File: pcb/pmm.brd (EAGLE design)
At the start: 30 x 35 mm, 12 parts, among them IC2 REG1117, IC3 STM32F042F4, U2 USBC_16P

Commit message: pcb done
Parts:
- removed JP15, JPAE: (no value), pinhead:1X05
- added C3, C5: 10uF, clock:0805@1
- added C4: 100nF, clock:0805@1
- added LED1, LED2: (no value), adafruit:CHIP-LED0805
- added R3, R5: 10K, joyAnalog:0805
- added R4, R7: 2K, SparkFun-Passives:0805
- added SW3, SW4: 324_SW, 3pos_slide_switch_centered:342_SWICH_FOOT
- added U$3, U$4, U$5, U$6: PINHD5, adafruit_changed:1X05
- C1: value 100nF -> 10uF
- JP1: device pinhead:1X06 -> adafruit:1X06-CLEANBIG
- moved JP1 29.9 mm to (2.16, 11.6), turned to 270 degrees
- moved R2 11.8 mm to (11.4, 25.0), turned to 0 degrees
- moved R1 3.70 mm to (3.43, 25.0), turned to 180 degrees
- moved U2 1.01 mm to (7.49, 31.1)
- moved C2 0.76 mm to (16.0, 28.6)
- moved IC2 0.38 mm to (22.0, 30.1)
- moved C1 0.18 mm to (16.0, 32.8), turned to 90 degrees
- turned IC3 to 180 degrees
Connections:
- removed net DNDNDN: U2.A7, U2.B7
- new net +5V: C1.2, C3.2, C5.2, IC2.3, JP1.5, R3.2, U$1.2, U$1.23, U$2.2, U$2.23, U$5.4, U2.A4B9, U2.B4A9
- new net BUTTON1: IC3.4, SW3.P$2, SW3.P$3
- new net BUTTON2: IC3.1, R5.2, SW4.P$2, SW4.P$3
- new net N$10: IC3.7, JP1.3
- new net N$11: IC3.6, JP1.4
- new net N$12: IC3.2, U$5.2
- new net N$13: IC3.3, U$5.3
- new net N$2: IC3.13, U$1.3
- new net N$29: LED2.C, R7.2
- new net N$3: U$1.22, U$2.3
- new net N$4: IC3.14, R3.1, U$1.24, U$2.24
- new net N$5: LED1.C, R4.2
- new net N$6: IC3.8, U$6.3
- new net N$7: IC3.20, U$6.1
- new net N$8: IC3.19, U$6.2
- new net N$9: IC3.9, JP1.2
- new net USB_DN: IC3.17, U2.A7, U2.B7
- new net USER_LED: IC3.10, R4.1
- net +3V3: now also C4.2, IC3.16, IC3.5, JP1.6, LED1.A, LED2.A, SW4.P$1, SW4.P$4, U$5.5, U$6.4; no longer JP1.4
- net 1: now also U$3.1; no longer JP15.1
- net 2: now also U$3.2; no longer JP15.2
- net 3: now also U$3.3; no longer JP15.3
- net 4: now also U$3.4; no longer JP15.4
- net 5: now also U$3.5; no longer JP15.5
- net A: now also U$4.1; no longer JPAE.1
- net B: now also U$4.2; no longer JPAE.2
- net C: now also U$4.3; no longer JPAE.3
- net E: now also U$4.5; no longer JPAE.5
- net GND: now also C3.1, C4.1, C5.1, IC3.15, JP1.1, R5.1, R7.1, SW3.P$1, SW3.P$4, U$1.21, U$1.4, U$2.21, U$2.4, U$5.1, U$6.5; no longer JP1.5
- net N$1: now also IC3.11, U$1.1, U$2.1; no longer C1.2, IC2.3, U2.A4B9, U2.B4A9
- net USB_DP: now also IC3.18
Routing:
- net +5V: track 0.00 -> 85.0 mm, vias 0 -> 1
- net GND: track 0.00 -> 47.9 mm
- net 3: track 0.00 -> 33.3 mm, vias 0 -> 1
- net 4: track 0.00 -> 30.4 mm, vias 0 -> 2
- net USB_DN: track 0.00 -> 28.8 mm
- net 5: track 0.00 -> 26.0 mm
- net 2: track 0.00 -> 25.6 mm, vias 0 -> 1
- net +3V3: track 0.00 -> 25.5 mm, vias 0 -> 6
- net USB_DP: track 0.00 -> 20.4 mm
- net A: track 0.00 -> 20.2 mm
- net N$13: track 0.00 -> 19.7 mm, vias 0 -> 1
- net E: track 0.00 -> 19.7 mm
- net 1: track 0.00 -> 19.3 mm
- net N$11: track 0.00 -> 18.9 mm, vias 0 -> 1
- net N$4: track 0.00 -> 18.8 mm, vias 0 -> 2
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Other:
- board text added: "1 2 3 4 5"
- board text added: "3"
- board text added: "5"
- board text added: "A B C D E"
- board text added: "A0"
- board text added: "A1"
- board text added: "A4"
- board text added: "C"
- board text added: "D"
- board text added: "F0"
- board text added: "F1"
- board text added: "G"
- board text added: "Pimp-my-microwave dekuNukem JUL2020 PT0"
- board text added: "RX"
- board text added: "T"

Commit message: minor cleanup
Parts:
- renumbered R7 to R6
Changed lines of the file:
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@@
 <setting verticaltext="up"/>
 </settings>
-<grid distance="5" unitdist="mil" unit="mil" style="lines" multiple="1" display="no" altdistance="1" altunitdist="mil" altunit="mil"/>
+<grid distance="5" unitdist="mil" unit="mm" style="lines" multiple="1" display="no" altdistance="1" altunitdist="mil" altunit="mil"/>
 <layers>
 <layer number="1" name="Top" color="4" fill="1" visible="yes" active="yes"/>
@@
 <attribute name="VALUE" x="2.159" y="20.574" size="1.27" layer="27"/>
 </element>
-<element name="R7" library="SparkFun-Passives" package="0805" value="2K" x="8.0518" y="23.495" smashed="yes" rot="R180">
+<element name="R6" library="SparkFun-Passives" package="0805" value="2K" x="8.0518" y="23.495" smashed="yes" rot="R180">
 <attribute name="NAME" x="8.6868" y="25.2095" size="0.8128" layer="25" rot="R180"/>
 </element>
@@
 <contactref element="C2" pad="2"/>
 <polygon width="0.1524" layer="1" isolate="0.254">
-<vertex x="0" y="35.052"/>
+<vertex x="0" y="35"/>
 <vertex x="0" y="0"/>
-<vertex x="29.972" y="0"/>
-<vertex x="29.972" y="35.052"/>
+<vertex x="30" y="0"/>
+<vertex x="30" y="35"/>
 </polygon>
 <contactref element="U$1" pad="4"/>
@@
 <contactref element="SW3" pad="P$1"/>
 <contactref element="SW3" pad="P$4"/>
-<contactref element="R7" pad="1"/>
+<contactref element="R6" pad="1"/>
 <contactref element="R5" pad="1"/>
 <contactref element="U$6" pad="5"/>
@@
 <contactref element="C2" pad="1"/>
 <polygon width="0.1524" layer="16">
-<vertex x="0" y="35.052"/>
-<vertex x="29.972" y="35.052"/>
-<vertex x="29.972" y="0"/>
+<vertex x="0" y="35"/>
+<vertex x="30" y="35"/>
+<vertex x="30" y="0"/>
 <vertex x="0" y="0"/>
 </polygon>
@@
 <signal name="N$29">
 <contactref element="LED2" pad="C"/>
-<contactref element="R7" pad="2"/>
+<contactref element="R6" pad="2"/>
 <wire x1="7.1518" y1="23.495" x2="6.7708" y2="23.114" width="0.1524" layer="1"/>
 <wire x1="6.7708" y1="23.114" x2="4.479" y2="23.114" width="0.1524" layer="1"/>

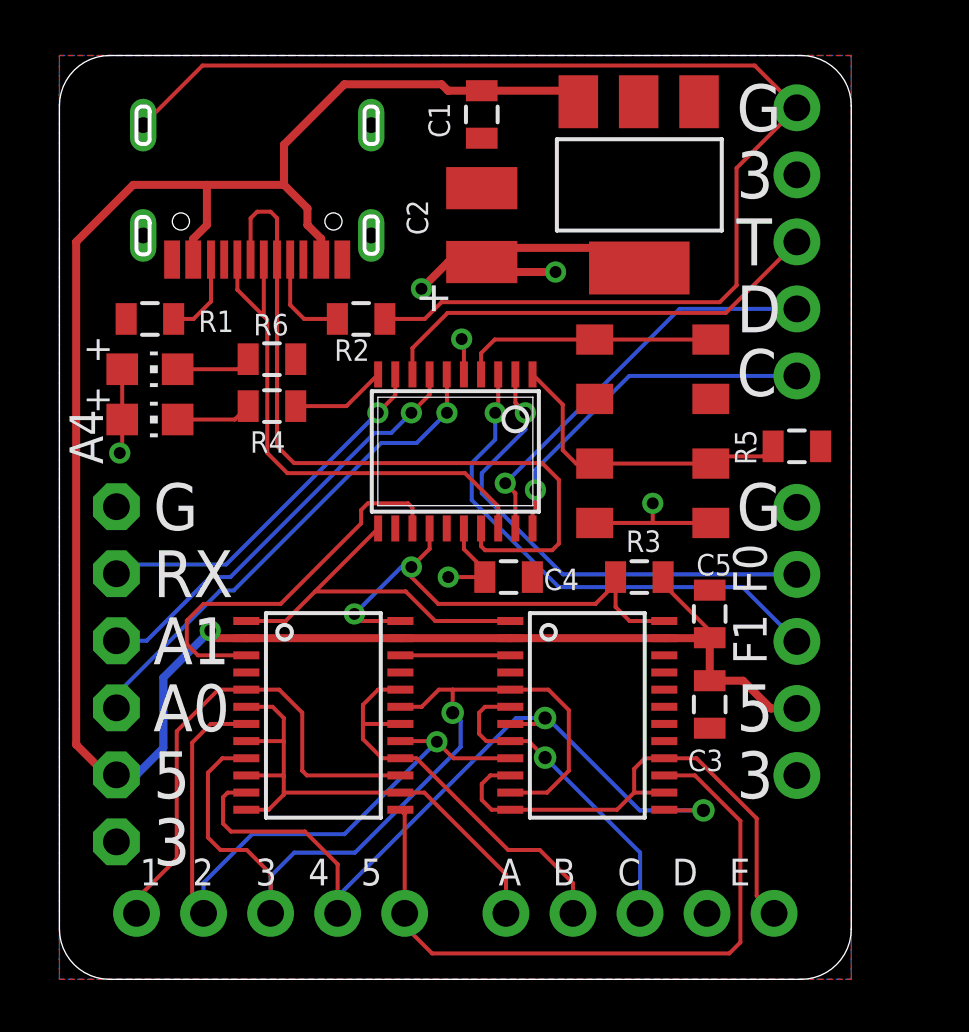
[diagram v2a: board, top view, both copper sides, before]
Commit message: added a required pullup resistor
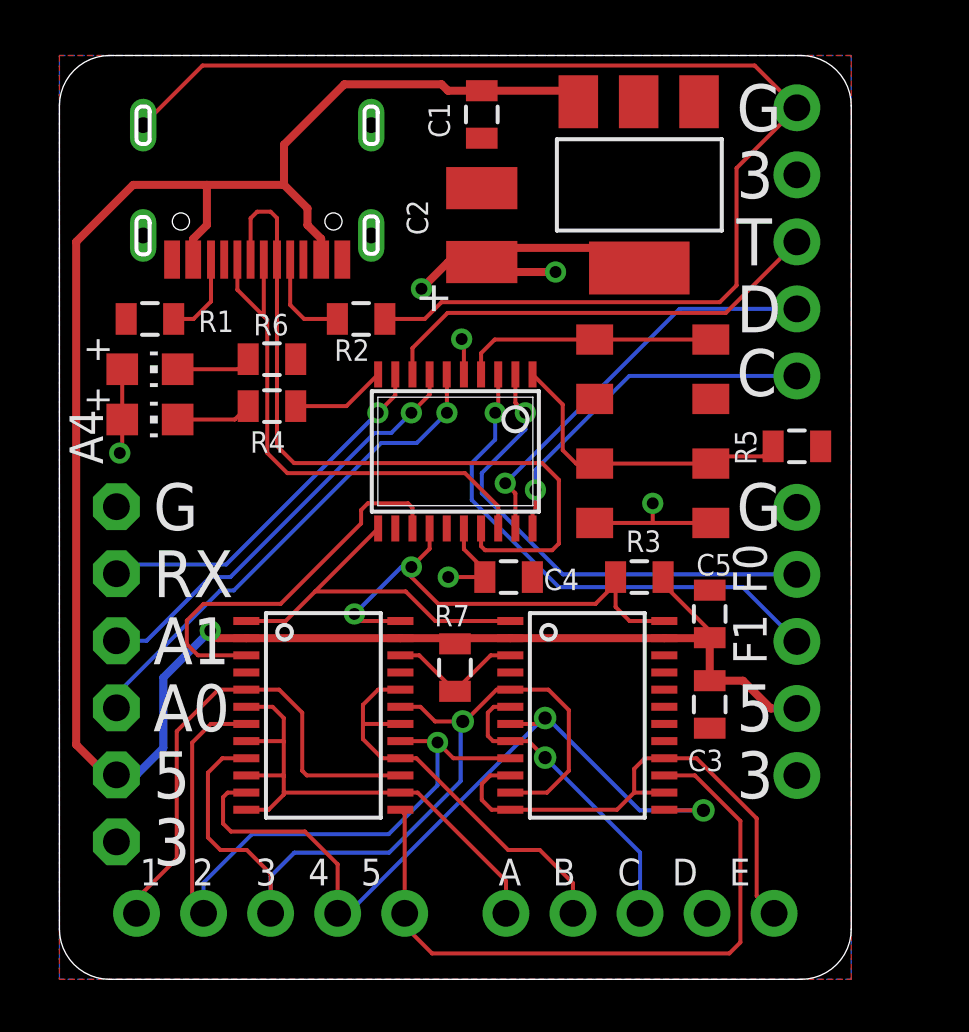
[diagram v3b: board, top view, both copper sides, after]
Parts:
- added R7: 10K, joyAnalog:0805
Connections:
- net +5V: now also R7.2
- net N$3: now also R7.1
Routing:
- net N$3: track 4.16 -> 5.30 mm
- net 2: track 25.6 -> 26.6 mm
- net C: track 12.3 -> 11.7 mm
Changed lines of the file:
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@@
 <setting verticaltext="up"/>
 </settings>
-<grid distance="5" unitdist="mil" unit="mm" style="lines" multiple="1" display="no" altdistance="1" altunitdist="mil" altunit="mil"/>
+<grid distance="1" unitdist="mil" unit="mil" style="lines" multiple="1" display="no" altdistance="1" altunitdist="mil" altunit="mil"/>
 <layers>
 <layer number="1" name="Top" color="4" fill="1" visible="yes" active="yes"/>
@@
 <attribute name="NAME" x="24.13" y="15.3035" size="0.8128" layer="25"/>
 </element>
+<element name="R7" library="joyAnalog" package="0805" value="10K" x="14.986" y="11.811" smashed="yes" rot="R90">
+<attribute name="NAME" x="15.5448" y="14.1859" size="0.8128" layer="25" rot="R180"/>
+</element>
 </elements>
 <signals>
@@
 <wire x1="12.9178" y1="7.075" x2="8.525" y2="7.075" width="0.1524" layer="1"/>
 <wire x1="8.525" y1="7.075" x2="8.5" y2="7.1" width="0.1524" layer="1"/>
-<wire x1="13.825" y1="7.075" x2="12.9178" y2="7.075" width="0.1524" layer="1"/>
-<wire x1="13.825" y1="7.075" x2="16.92" y2="3.98" width="0.1524" layer="1"/>
+<wire x1="13.571" y1="7.075" x2="12.9178" y2="7.075" width="0.1524" layer="1"/>
+<wire x1="13.571" y1="7.075" x2="16.92" y2="3.726" width="0.1524" layer="1"/>
 <contactref element="U$4" pad="1"/>
-<wire x1="16.92" y1="3.98" x2="16.92" y2="2.5036" width="0.1524" layer="1"/>
+<wire x1="16.92" y1="3.726" x2="16.92" y2="2.5036" width="0.1524" layer="1"/>
 <wire x1="16.92" y1="2.5036" x2="16.9164" y2="2.5" width="0.1524" layer="1"/>
 </signal>
@@
 <contactref element="U$2" pad="6"/>
 <contactref element="U$2" pad="8"/>
-<wire x1="17.0822" y1="10.325" x2="16.125" y2="10.325" width="0.1524" layer="1"/>
-<wire x1="16.125" y1="10.325" x2="15.9" y2="10.1" width="0.1524" layer="1"/>
-<wire x1="15.9" y1="10.1" x2="15.9" y2="9.3" width="0.1524" layer="1"/>
-<wire x1="16.175" y1="9.025" x2="17.0822" y2="9.025" width="0.1524" layer="1"/>
-<wire x1="15.9" y1="9.3" x2="16.175" y2="9.025" width="0.1524" layer="1"/>
+<wire x1="17.0822" y1="10.325" x2="16.4552" y2="10.325" width="0.1524" layer="1"/>
+<wire x1="16.4552" y1="10.325" x2="16.2302" y2="10.1" width="0.1524" layer="1"/>
+<wire x1="16.2302" y1="10.1" x2="16.2302" y2="9.2238" width="0.1524" layer="1"/>
+<wire x1="16.429" y1="9.025" x2="17.0822" y2="9.025" width="0.1524" layer="1"/>
+<wire x1="16.2302" y1="9.2238" x2="16.429" y2="9.025" width="0.1524" layer="1"/>
 <wire x1="17.0822" y1="9.025" x2="17.775" y2="9.025" width="0.1524" layer="1"/>
 <wire x1="17.775" y1="9.025" x2="18.4" y2="8.4" width="0.1524" layer="1"/>
@@
 <contactref element="U$1" pad="17"/>
 <contactref element="U$2" pad="9"/>
-<via x="14.3" y="9" extent="1-16" drill="0.45"/>
-<wire x1="14.3" y1="9" x2="10.8" y2="5.5" width="0.1524" layer="16"/>
-<wire x1="10.8" y1="5.5" x2="7.3" y2="5.5" width="0.1524" layer="16"/>
+<via x="14.3254" y="8.9746" extent="1-16" drill="0.45"/>
+<wire x1="14.3254" y1="8.9746" x2="14.3254" y2="7.349" width="0.1524" layer="16"/>
+<wire x1="14.3254" y1="7.349" x2="12.4764" y2="5.5" width="0.1524" layer="16"/>
+<wire x1="12.4764" y1="5.5" x2="7.3" y2="5.5" width="0.1524" layer="16"/>
 <wire x1="7.3" y1="5.5" x2="5.46" y2="3.66" width="0.1524" layer="16"/>
 <wire x1="12.9178" y1="9.025" x2="14.275" y2="9.025" width="0.1524" layer="1"/>
-<wire x1="14.275" y1="9.025" x2="14.3" y2="9" width="0.1524" layer="1"/>
-<wire x1="14.925" y1="8.375" x2="14.3" y2="9" width="0.1524" layer="1"/>
+<wire x1="14.275" y1="9.025" x2="14.3254" y2="8.9746" width="0.1524" layer="1"/>
+<wire x1="14.925" y1="8.375" x2="14.3254" y2="8.9746" width="0.1524" layer="1"/>
 <wire x1="17.0822" y1="8.375" x2="14.925" y2="8.375" width="0.1524" layer="1"/>
 <wire x1="7.0822" y1="9.675" x2="5.738" y2="9.675" width="0.1524" layer="1"/>
@@
 <wire x1="5.627" y1="5.373" x2="6.1" y2="4.9" width="0.1524" layer="1"/>
 <wire x1="6.1" y1="4.9" x2="7.1" y2="4.9" width="0.1524" layer="1"/>
-<wire x1="17.0822" y1="10.975" x2="14.9" y2="10.975" width="0.1524" layer="1"/>
-<wire x1="14.9" y1="10.975" x2="14.375" y2="10.975" width="0.1524" layer="1"/>
-<wire x1="13.725" y1="10.325" x2="12.9178" y2="10.325" width="0.1524" layer="1"/>
-<wire x1="14.375" y1="10.975" x2="13.725" y2="10.325" width="0.1524" layer="1"/>
 <wire x1="17.0822" y1="7.075" x2="18.475" y2="7.075" width="0.1524" layer="1"/>
 <wire x1="18.475" y1="7.075" x2="19.3" y2="7.9" width="0.1524" layer="1"/>
@@
 <wire x1="18.525" y1="10.975" x2="17.0822" y2="10.975" width="0.1524" layer="1"/>
 <wire x1="19.3" y1="10.2" x2="18.525" y2="10.975" width="0.1524" layer="1"/>
-<wire x1="14.9" y1="10.975" x2="14.9" y2="10.1" width="0.1524" layer="1"/>
-<via x="14.9" y="10.1" extent="1-16" drill="0.5"/>
-<wire x1="14.9" y1="10.1" x2="15.2" y2="9.8" width="0.1524" layer="16"/>
-<wire x1="15.2" y1="9.8" x2="15.2" y2="8.8" width="0.1524" layer="16"/>
-<wire x1="15.2" y1="8.8" x2="11.2" y2="4.8" width="0.1524" layer="16"/>
-<wire x1="11.2" y1="4.8" x2="8.9" y2="4.8" width="0.1524" layer="16"/>
+<via x="15.281" y="9.7698" extent="1-16" drill="0.5"/>
+<wire x1="15.281" y1="9.7698" x2="15.2" y2="9.6888" width="0.1524" layer="16"/>
+<wire x1="15.2" y1="9.6888" x2="15.2" y2="7.5046" width="0.1524" layer="16"/>
+<wire x1="15.2" y1="7.5046" x2="12.4954" y2="4.8" width="0.1524" layer="16"/>
+<wire x1="12.4954" y1="4.8" x2="8.9" y2="4.8" width="0.1524" layer="16"/>
 <wire x1="8.9" y1="4.8" x2="8" y2="3.9" width="0.1524" layer="16"/>
 <contactref element="U$3" pad="3"/>
@@
 <wire x1="8" y1="2.501" x2="8.001" y2="2.5" width="0.1524" layer="16"/>
 <wire x1="8.001" y1="3.999" x2="8.001" y2="2.5" width="0.1524" layer="1"/>
+<wire x1="12.9178" y1="10.325" x2="13.678" y2="10.325" width="0.1524" layer="1"/>
+<wire x1="14.2332" y1="9.7698" x2="15.281" y2="9.7698" width="0.1524" layer="1"/>
+<wire x1="13.678" y1="10.325" x2="14.2332" y2="9.7698" width="0.1524" layer="1"/>
+<wire x1="17.0822" y1="10.975" x2="16.563" y2="10.975" width="0.1524" layer="1"/>
+<wire x1="15.3578" y1="9.7698" x2="15.281" y2="9.7698" width="0.1524" layer="1"/>
+<wire x1="16.563" y1="10.975" x2="15.3578" y2="9.7698" width="0.1524" layer="1"/>
 </signal>
 <signal name="4">
@@
 <wire x1="24.4" y1="6.4" x2="22.9428" y2="6.4" width="0.1524" layer="1"/>
 <wire x1="22.9428" y1="6.4" x2="22.9178" y2="6.425" width="0.1524" layer="1"/>
-<wire x1="17.3" y1="9.9" x2="18.4" y2="9.9" width="0.1524" layer="16"/>
-<wire x1="10.54" y1="3.14" x2="17.3" y2="9.9" width="0.1524" layer="16"/>
+<wire x1="18.3414" y1="9.9" x2="18.4" y2="9.9" width="0.1524" layer="16"/>
+<wire x1="18.3414" y1="9.9" x2="10.9414" y2="2.5" width="0.1524" layer="16"/>
+<wire x1="10.541" y1="2.5" x2="10.9414" y2="2.5" width="0.1524" layer="16"/>
 <contactref element="U$3" pad="4"/>
 <wire x1="9.3" y1="5.6" x2="10.541" y2="4.359" width="0.1524" layer="1"/>
 <wire x1="10.541" y1="4.359" x2="10.541" y2="2.5" width="0.1524" layer="1"/>
-<wire x1="10.541" y1="2.5" x2="10.541" y2="3.139" width="0.1524" layer="16"/>
-<wire x1="10.541" y1="3.139" x2="10.54" y2="3.14" width="0.1524" layer="16"/>
 </signal>
 <signal name="5">
@@
 <wire x1="1.778" y1="7.747" x2="2.159" y2="7.747" width="0.3048" layer="1"/>
 <wire x1="22.9178" y1="12.925" x2="17.0822" y2="12.925" width="0.3048" layer="1"/>
-<wire x1="17.0822" y1="12.925" x2="12.9178" y2="12.925" width="0.3048" layer="1"/>
 <wire x1="12.9178" y1="12.925" x2="7.0822" y2="12.925" width="0.3048" layer="1"/>
 <wire x1="7.0822" y1="12.925" x2="5.998" y2="12.925" width="0.3048" layer="1"/>
@@
 <wire x1="24.638" y1="13.208" x2="24.638" y2="12.943" width="0.1524" layer="1"/>
 <wire x1="22.871" y1="14.975" x2="24.638" y2="13.208" width="0.1524" layer="1"/>
+<contactref element="R7" pad="2"/>
+<wire x1="12.9178" y1="12.925" x2="14.772" y2="12.925" width="0.3048" layer="1"/>
+<wire x1="14.772" y1="12.925" x2="14.986" y2="12.711" width="0.3048" layer="1"/>
+<wire x1="17.0822" y1="12.925" x2="15.2" y2="12.925" width="0.3048" layer="1"/>
+<wire x1="15.2" y1="12.925" x2="14.986" y2="12.711" width="0.3048" layer="1"/>
 </signal>
 <signal name="N$1">
@@
 <contactref element="U$1" pad="22"/>
 <contactref element="U$2" pad="3"/>
-<wire x1="12.9178" y1="12.275" x2="17.0822" y2="12.275" width="0.1524" layer="1"/>
+<contactref element="R7" pad="1"/>
+<wire x1="12.9178" y1="12.275" x2="13.633" y2="12.275" width="0.1524" layer="1"/>
+<wire x1="14.986" y1="10.922" x2="14.986" y2="10.911" width="0.1524" layer="1"/>
+<wire x1="13.633" y1="12.275" x2="14.986" y2="10.922" width="0.1524" layer="1"/>
+<wire x1="17.0822" y1="12.275" x2="16.339" y2="12.275" width="0.1524" layer="1"/>
+<wire x1="16.339" y1="12.275" x2="14.986" y2="10.922" width="0.1524" layer="1"/>
 </signal>
 <signal name="N$4">

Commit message: 2nd prototype
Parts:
- moved R7 0.13 mm to (15.0, 11.9)
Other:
- board text added: "Pimp-my-microwave dekuNukem AUG2020 PT1"
- board text removed: "Pimp-my-microwave dekuNukem JUL2020 PT0"
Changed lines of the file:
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@@
 <text x="10.922" y="27.94" size="1.778" layer="22" rot="MR270">Pimp-my-microwave
 dekuNukem
-JUL2020 PT0</text>
+AUG2020 PT1</text>
 </plain>
 <attributes>
@@
 <attribute name="NAME" x="24.13" y="15.3035" size="0.8128" layer="25"/>
 </element>
-<element name="R7" library="joyAnalog" package="0805" value="10K" x="14.986" y="11.811" smashed="yes" rot="R90">
-<attribute name="NAME" x="15.5448" y="14.1859" size="0.8128" layer="25" rot="R180"/>
+<element name="R7" library="joyAnalog" package="0805" value="10K" x="14.986" y="11.938" smashed="yes" rot="R90">
+<attribute name="NAME" x="15.5448" y="14.3129" size="0.8128" layer="25" rot="R180"/>
 </element>
 </elements>
@@
 <wire x1="22.871" y1="14.975" x2="24.638" y2="13.208" width="0.1524" layer="1"/>
 <contactref element="R7" pad="2"/>
-<wire x1="12.9178" y1="12.925" x2="14.772" y2="12.925" width="0.3048" layer="1"/>
-<wire x1="14.772" y1="12.925" x2="14.986" y2="12.711" width="0.3048" layer="1"/>
-<wire x1="17.0822" y1="12.925" x2="15.2" y2="12.925" width="0.3048" layer="1"/>
-<wire x1="15.2" y1="12.925" x2="14.986" y2="12.711" width="0.3048" layer="1"/>
+<wire x1="12.9178" y1="12.925" x2="14.899" y2="12.925" width="0.3048" layer="1"/>
+<wire x1="14.899" y1="12.925" x2="14.986" y2="12.838" width="0.3048" layer="1"/>
+<wire x1="17.0822" y1="12.925" x2="15.073" y2="12.925" width="0.3048" layer="1"/>
+<wire x1="15.073" y1="12.925" x2="14.986" y2="12.838" width="0.3048" layer="1"/>
 </signal>
 <signal name="N$1">
@@
 <wire x1="9.6884" y1="14.6956" x2="8.5678" y2="13.575" width="0.1524" layer="1"/>
 <wire x1="8.5678" y1="13.575" x2="7.0822" y2="13.575" width="0.1524" layer="1"/>
-<wire x1="17.0822" y1="13.575" x2="14.238" y2="13.575" width="0.1524" layer="1"/>
+<wire x1="17.0822" y1="13.575" x2="17.006" y2="13.6512" width="0.1524" layer="1"/>
+<wire x1="17.006" y1="13.6512" x2="14.1618" y2="13.6512" width="0.1524" layer="1"/>
 <wire x1="13.1174" y1="14.6956" x2="9.6884" y2="14.6956" width="0.1524" layer="1"/>
-<wire x1="14.238" y1="13.575" x2="13.1174" y2="14.6956" width="0.1524" layer="1"/>
+<wire x1="14.1618" y1="13.6512" x2="13.1174" y2="14.6956" width="0.1524" layer="1"/>
 </signal>
 <signal name="N$2">
@@
 <contactref element="R7" pad="1"/>
 <wire x1="12.9178" y1="12.275" x2="13.633" y2="12.275" width="0.1524" layer="1"/>
-<wire x1="14.986" y1="10.922" x2="14.986" y2="10.911" width="0.1524" layer="1"/>
+<wire x1="14.986" y1="10.922" x2="14.986" y2="11.038" width="0.1524" layer="1"/>
 <wire x1="13.633" y1="12.275" x2="14.986" y2="10.922" width="0.1524" layer="1"/>
 <wire x1="17.0822" y1="12.275" x2="16.339" y2="12.275" width="0.1524" layer="1"/>
